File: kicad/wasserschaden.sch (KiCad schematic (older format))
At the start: 16 parts, among them J1 valve out, J2 12V in, J3 sense, U1 stepdown, U2 WeMos_mini

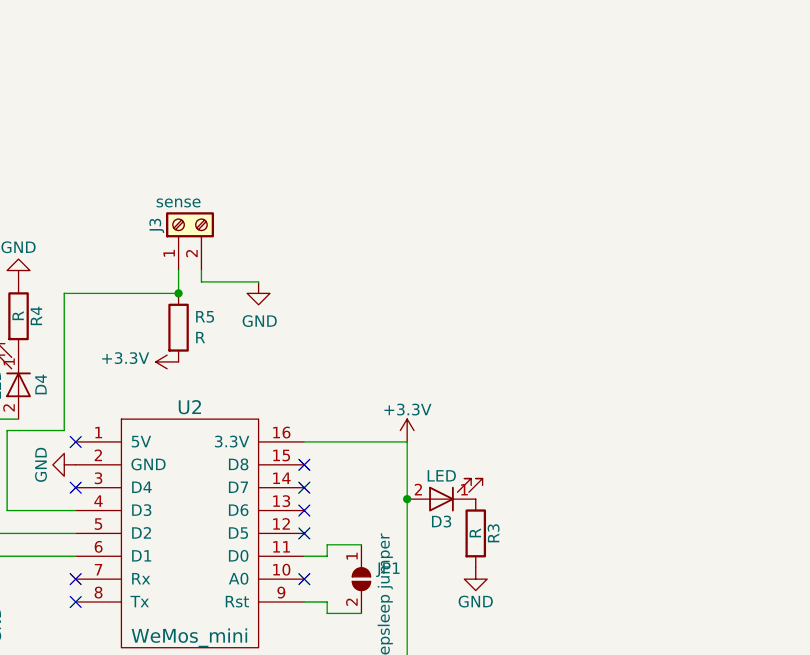
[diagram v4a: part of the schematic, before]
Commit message: added temperature sensor
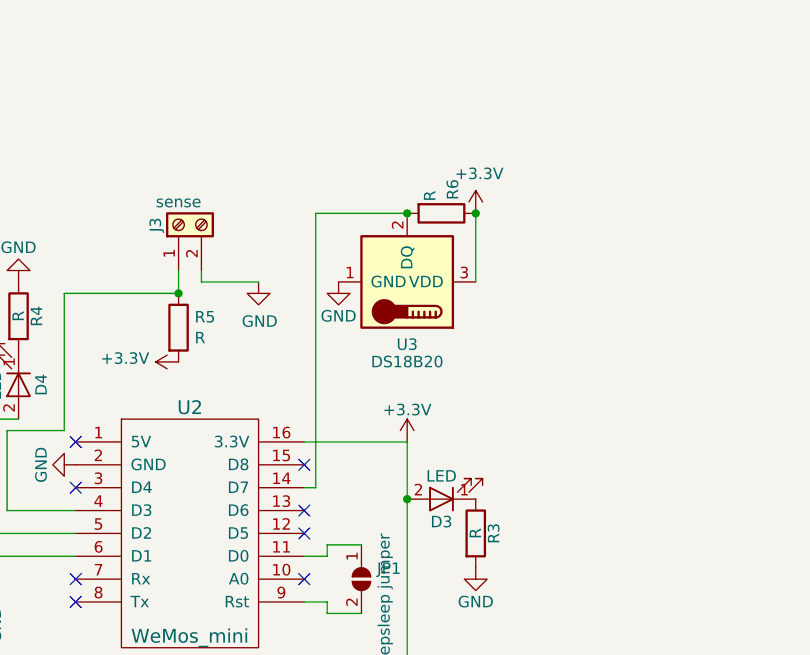
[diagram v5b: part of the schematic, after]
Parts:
- added R6: R, Resistors_THT:R_Axial_DIN0207_L6.3mm_D2.5mm_P7.62mm_Horizontal, symbol Device:R
- added U3: DS18B20, custom:temperature_sensor, symbol Sensor_Temperature:DS18B20
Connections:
- net +3V3: now also R6.1, U3.3 (VDD)
- net GND: now also U3.1 (GND)
- net at U2.14 (D7): now also R6.2, U3.2 (DQ)
- no-connect marks 11 -> 10
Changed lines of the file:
@@
 NoConn ~ 4500 2350
 NoConn ~ 4500 2050
-NoConn ~ 4500 1950
 NoConn ~ 4500 1850
 Wire Wire Line
@@
 Wire Wire Line
 	4950 2000 4950 3050
+$Comp
+L Sensor_Temperature:DS18B20 U3
+U 1 1 5C092FAF
+P 4950 1050
+F 0 "U3" V 4676 1050 50  0000 C CNN
+F 1 "DS18B20" V 4600 1050 50  0000 C CNN
+F 2 "custom:temperature_sensor" H 3950 800 50  0001 C CNN
+F 3 "http://datasheets.maximintegrated.com/en/ds/DS18B20.pdf" H 4800 1300 50  0001 C CNN
+	1    4950 1050
+	0    1    -1   0
+$EndComp
+$Comp
+L power:+3.3V #PWR015
+U 1 1 5C093158
+P 5250 750
+F 0 "#PWR015" H 5250 600 50  0001 C CNN
+F 1 "+3.3V" H 5265 923 50  0000 C CNN
+F 2 "" H 5250 750 50  0001 C CNN
+F 3 "" H 5250 750 50  0001 C CNN
+	1    5250 750
+	1    0    0    -1
+$EndComp
+$Comp
+L power:GND #PWR014
+U 1 1 5C0931D7
+P 4650 1050
+F 0 "#PWR014" H 4650 800 50  0001 C CNN
+F 1 "GND" H 4650 900 50  0000 C CNN
+F 2 "" H 4650 1050 50  0001 C CNN
+F 3 "" H 4650 1050 50  0001 C CNN
+	1    4650 1050
+	1    0    0    -1
+$EndComp
+$Comp
+L Device:R R6
+U 1 1 5C09361D
+P 5100 750
+F 0 "R6" H 4950 800 50  0000 L CNN
+F 1 "R" H 5000 700 50  0000 L CNN
+F 2 "Resistors_THT:R_Axial_DIN0207_L6.3mm_D2.5mm_P7.62mm_Horizontal" V 5030 750 50  0001 C CNN
+F 3 "~" H 5100 750 50  0001 C CNN
+	1    5100 750
+	0    1    1    0
+$EndComp
+Wire Wire Line
+	5250 1050 5250 750
+Connection ~ 5250 750
+Wire Wire Line
+	4500 1950 4550 1950
+Wire Wire Line
+	4550 1950 4550 750
+Wire Wire Line
+	4550 750  4950 750
+Connection ~ 4950 750
 $EndSCHEMATC

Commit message: added R values, improved stepdown footprint, rerouted resistors
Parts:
- D2: value LED -> valve
- D4: value LED -> info
- JP1: value deepsleep jumper -> deepsleep
- R2, R3: value R -> 1K
- R4: value R -> 240
- R5: value R -> 330
- R6: value R -> 4K7
- U1: symbol wasserschaden-cache-2018-10-17-20-35-24:stepdown -> wasserschaden-rescue:stepdown-wasserschaden-cache-2018-10-17-20-35-24
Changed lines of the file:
@@
 $EndComp
 $Comp
-L wasserschaden-cache-2018-10-17-20-35-24:stepdown U1
+L wasserschaden-rescue:stepdown-wasserschaden-cache-2018-10-17-20-35-24 U1
 U 1 1 5B2A6F8D
 P 3800 3000
@@
 P 3000 1500
 F 0 "D2" H 3000 1600 50  0000 C CNN
-F 1 "LED" H 3000 1400 50  0000 C CNN
+F 1 "valve" H 3000 1400 50  0000 C CNN
 F 2 "LEDs:LED_D3.0mm" H 3000 1500 50  0001 C CNN
 F 3 "" H 3000 1500 50  0001 C CNN
@@
 P 3000 1200
 F 0 "R2" V 3080 1200 50  0000 C CNN
-F 1 "R" V 3000 1200 50  0000 C CNN
+F 1 "1K" V 3000 1200 50  0000 C CNN
 F 2 "Resistors_THT:R_Axial_DIN0207_L6.3mm_D2.5mm_P7.62mm_Horizontal" V 2930 1200 50  0001 C CNN
 F 3 "" H 3000 1200 50  0001 C CNN
@@
 P 5250 2150
 F 0 "R3" V 5330 2150 50  0000 C CNN
-F 1 "R" V 5250 2150 50  0000 C CNN
+F 1 "1K" V 5250 2150 50  0000 C CNN
 F 2 "Resistors_THT:R_Axial_DIN0207_L6.3mm_D2.5mm_P7.62mm_Horizontal" V 5180 2150 50  0001 C CNN
 F 3 "" H 5250 2150 50  0001 C CNN
@@
 P 3250 1500
 F 0 "D4" H 3250 1600 50  0000 C CNN
-F 1 "LED" H 3250 1400 50  0000 C CNN
+F 1 "info" H 3250 1400 50  0000 C CNN
 F 2 "LEDs:LED_D3.0mm" H 3250 1500 50  0001 C CNN
 F 3 "" H 3250 1500 50  0001 C CNN
@@
 P 3250 1200
 F 0 "R4" V 3330 1200 50  0000 C CNN
-F 1 "R" V 3250 1200 50  0000 C CNN
+F 1 "240" V 3250 1200 50  0000 C CNN
 F 2 "Resistors_THT:R_Axial_DIN0207_L6.3mm_D2.5mm_P7.62mm_Horizontal" V 3180 1200 50  0001 C CNN
 F 3 "" H 3250 1200 50  0001 C CNN
@@
 P 4750 2350
 F 0 "JP1" V 4704 2418 50  0000 L CNN
-F 1 "deepsleep jumper" H 4550 2450 50  0000 L CNN
+F 1 "deepsleep" H 4550 2450 50  0000 L CNN
 F 2 "custom:jumper" H 4750 2350 50  0001 C CNN
 F 3 "~" H 4750 2350 50  0001 C CNN
@@
 P 3950 1250
 F 0 "R5" H 4020 1296 50  0000 L CNN
-F 1 "R" H 4020 1205 50  0000 L CNN
+F 1 "330" H 4020 1205 50  0000 L CNN
 F 2 "Resistors_THT:R_Axial_DIN0207_L6.3mm_D2.5mm_P7.62mm_Horizontal" V 3880 1250 50  0001 C CNN
 F 3 "~" H 3950 1250 50  0001 C CNN
@@
 P 5100 750
 F 0 "R6" H 4950 800 50  0000 L CNN
-F 1 "R" H 5000 700 50  0000 L CNN
+F 1 "4K7" H 5000 700 50  0000 L CNN
 F 2 "Resistors_THT:R_Axial_DIN0207_L6.3mm_D2.5mm_P7.62mm_Horizontal" V 5030 750 50  0001 C CNN
 F 3 "~" H 5100 750 50  0001 C CNN
